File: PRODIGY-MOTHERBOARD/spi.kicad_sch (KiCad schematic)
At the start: 0 parts

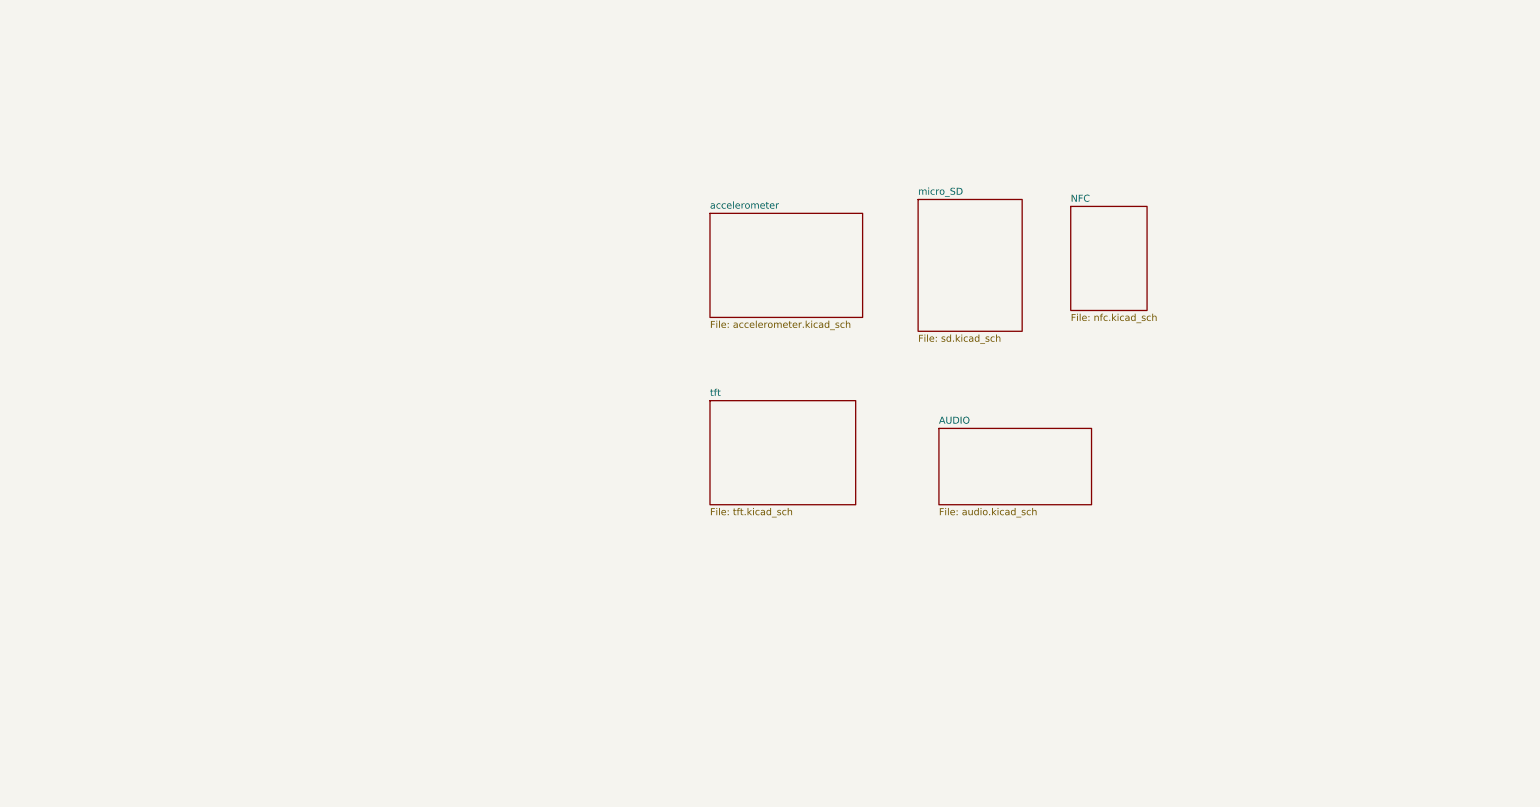
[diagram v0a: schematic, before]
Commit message: Finished I2C device and bus schematics. Added logic level translation.
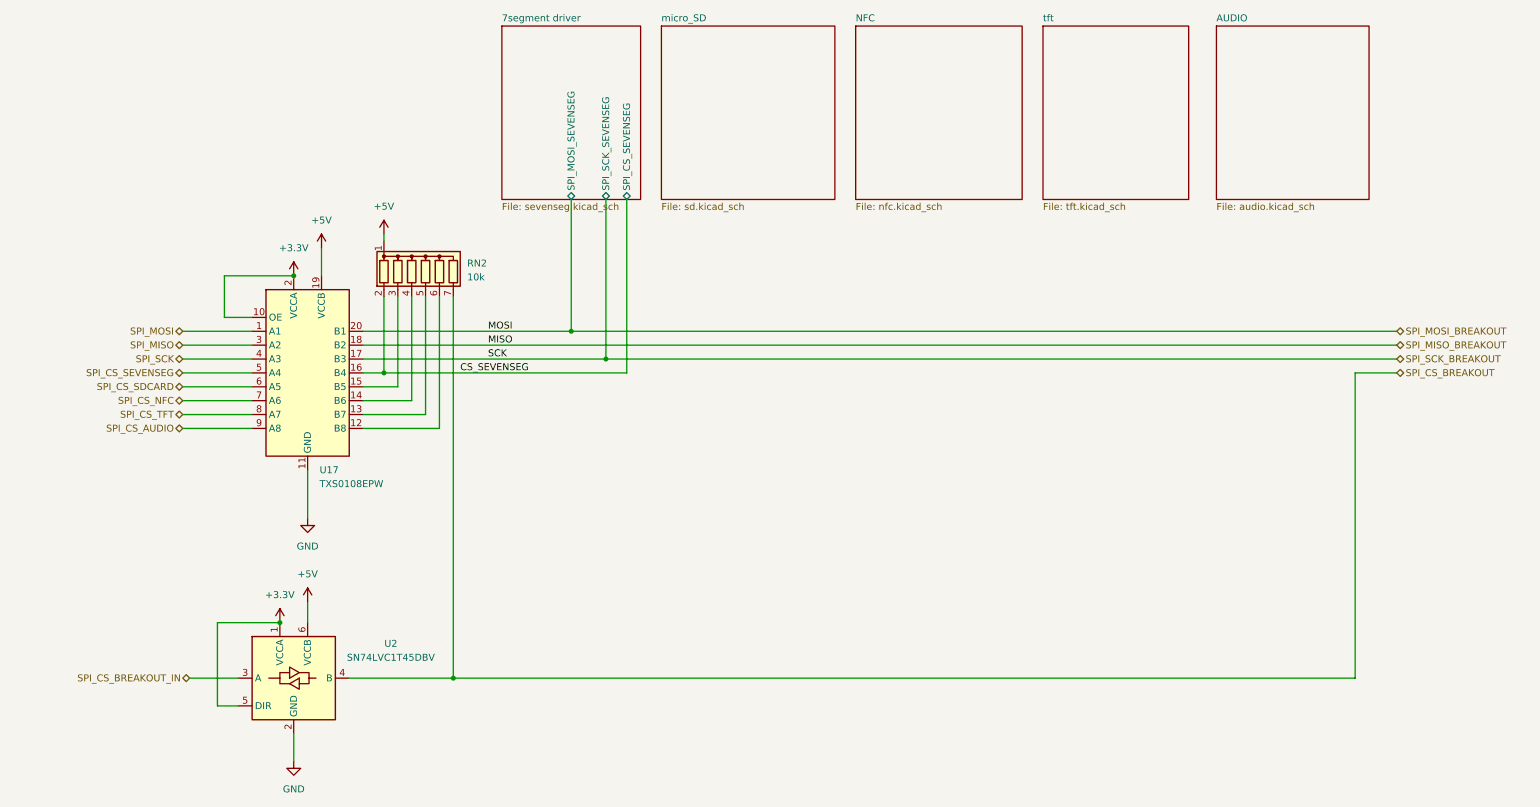
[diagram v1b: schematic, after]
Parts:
- added RN2: 10k, Resistor_SMD:R_Array_Convex_4x0603, symbol Device:R_Network06
- added U17: TXS0108EPW, Package_SO:TSSOP-20_4.4x6.5mm_P0.65mm, symbol Logic_LevelTranslator:TXS0108EPW
- added U2: SN74LVC1T45DBV, Package_TO_SOT_SMD:SOT-23-6, symbol Logic_LevelTranslator:SN74LVC1T45DBV
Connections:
- new net: RN2.6 (R5), U17.12 (B8)
- new net: RN2.5 (R4), U17.13 (B7)
- new net: RN2.4 (R3), U17.14 (B6)
- new net: RN2.3 (R2), U17.15 (B5)
- new net +3.3V: U17.10 (OE), U17.2 (VCCA), U2.1 (VCCA), U2.5 (DIR)
- new net +5V: RN2.1 (common), U17.19 (VCCB), U2.6 (VCCB)
- new net CS_SEVENSEG: RN2.2 (R1), U17.16 (B4)
- new net GND: U17.11 (GND), U2.2 (GND)
- new net SPI_CS_AUDIO: U17.9 (A8)
- new net SPI_CS_BREAKOUT: RN2.7 (R6), U2.4 (B)
- new net SPI_CS_BREAKOUT_IN: U2.3 (A)
- new net SPI_CS_NFC: U17.7 (A6)
- new net SPI_CS_SDCARD: U17.6 (A5)
- new net SPI_CS_SEVENSEG: U17.5 (A4)
- new net SPI_CS_TFT: U17.8 (A7)
- new net SPI_MISO: U17.3 (A2)
- new net SPI_MISO_BREAKOUT: U17.18 (B2)
- new net SPI_MOSI: U17.1 (A1)
- new net SPI_MOSI_BREAKOUT: U17.20 (B1)
- new net SPI_SCK: U17.4 (A3)
- new net SPI_SCK_BREAKOUT: U17.17 (B3)
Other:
- removed sheet accelerometer
- added sheet 7segment driver (sevenseg.kicad_sch)

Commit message: SPI SD CARD circuit added.
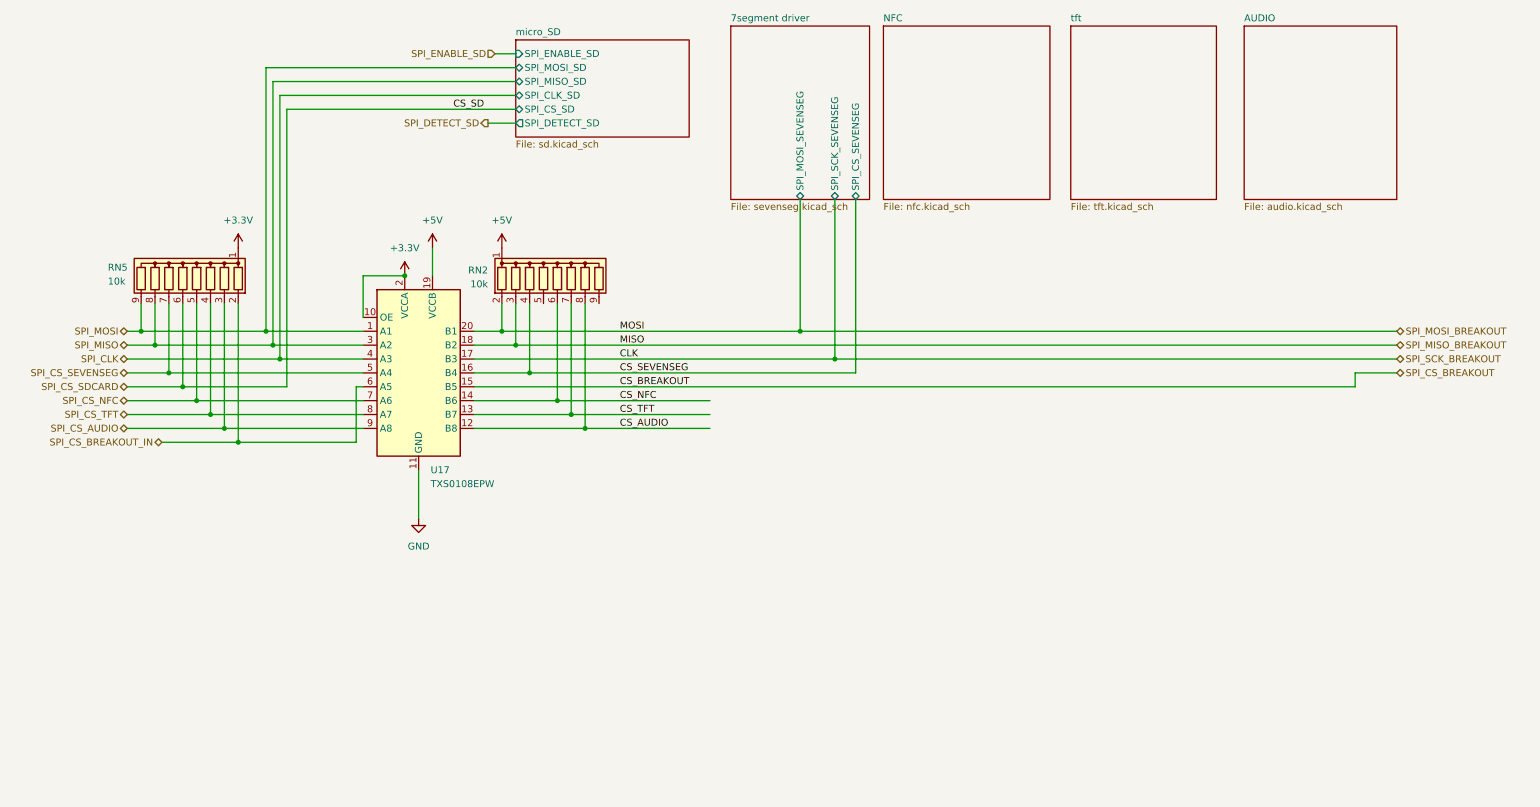
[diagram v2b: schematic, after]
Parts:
- removed RN2: 10k, Resistor_SMD:R_Array_Convex_4x0603, symbol Device:R_Network06
- removed U2: SN74LVC1T45DBV, Package_TO_SOT_SMD:SOT-23-6, symbol Logic_LevelTranslator:SN74LVC1T45DBV
- added RN2, RN5: 10k, Resistor_SMD:R_Array_Convex_5x0603, symbol Device:R_Network08
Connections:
- net +3.3V: now also RN5.1 (common)
- net +5V: now also RN2.1 (common)
- net CS_SEVENSEG: now also RN2.4 (R3)
- net SPI_CS_AUDIO: now also RN5.3 (R2)
- net SPI_CS_BREAKOUT: now also U17.15 (B5)
- net SPI_CS_BREAKOUT_IN: now also U17.6 (A5), RN5.2 (R1)
- net SPI_CS_NFC: now also RN5.5 (R4)
- net SPI_CS_SDCARD: now also RN5.6 (R5); no longer U17.6 (A5)
- net SPI_CS_SEVENSEG: now also RN5.7 (R6)
- net SPI_CS_TFT: now also RN5.4 (R3)
- net SPI_MISO: now also RN5.8 (R7)
- net SPI_MISO_BREAKOUT: now also RN2.3 (R2)
- net SPI_MOSI: now also RN5.9 (R8)
- net SPI_MOSI_BREAKOUT: now also RN2.2 (R1)
- net CS_AUDIO: now reaches U17.12 (B8)
- net CS_AUDIO: now also RN2.8 (R7)
- net CS_TFT: now reaches U17.13 (B7)
- net CS_TFT: now also RN2.7 (R6)
- net CS_NFC: now reaches U17.14 (B6)
- net CS_NFC: now also RN2.6 (R5)
- net SPI_SCK renamed SPI_CLK
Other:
- sheet micro_SD ports: added SPI_CLK_SD, SPI_CS_SD, SPI_DETECT_SD, SPI_ENABLE_SD, SPI_MISO_SD, SPI_MOSI_SD; removed none
- moved on the sheet: U17

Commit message: Finished neopixel and button's schematic.
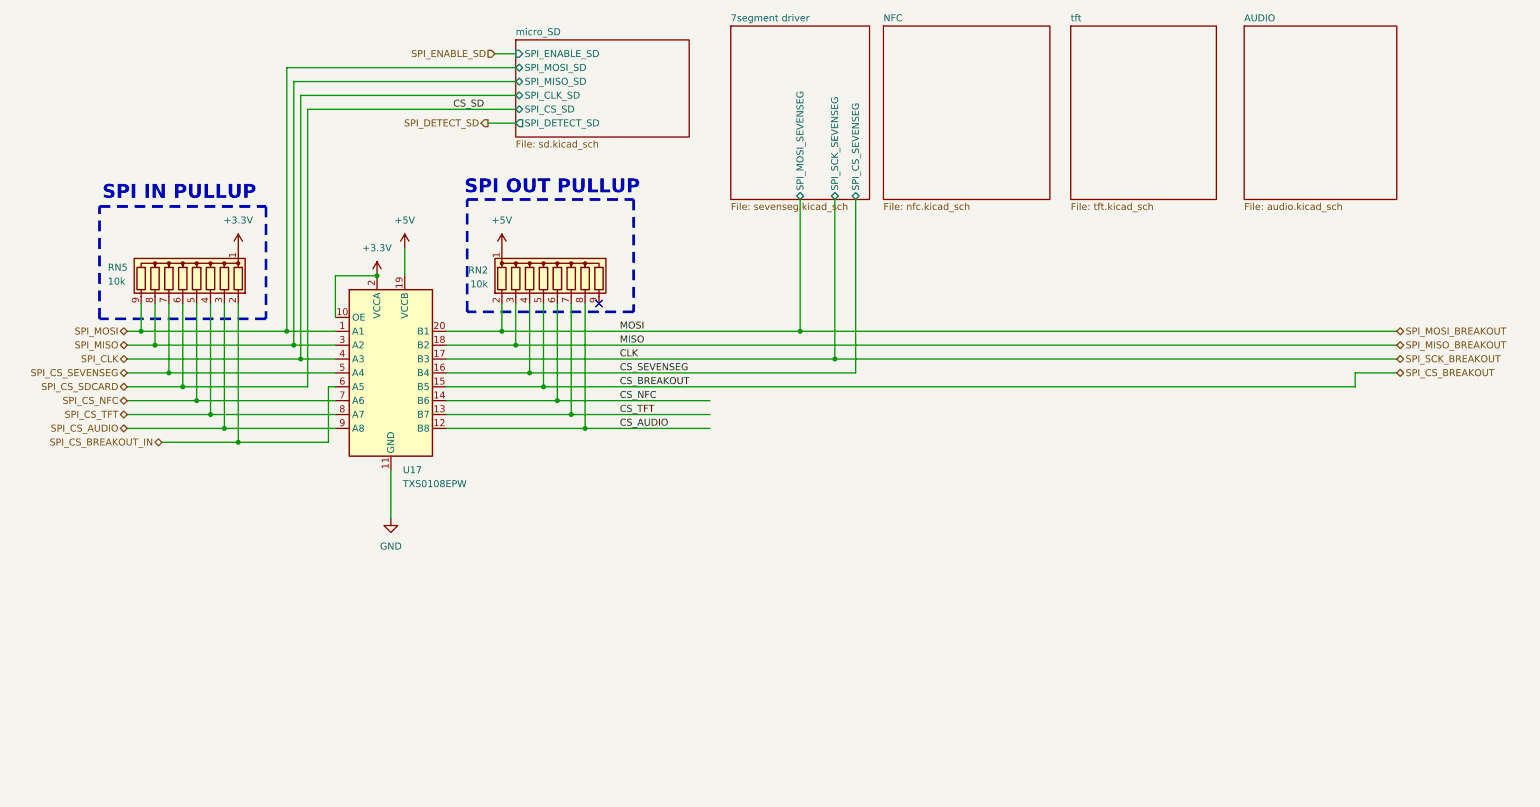
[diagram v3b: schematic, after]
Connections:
- net SPI_CS_BREAKOUT: now also RN2.5 (R4)
- no-connect marks 0 -> 1
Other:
- note added: "SPI IN PULLUP"
- note added: "SPI OUT PULLUP"
- moved on the sheet: U17

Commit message: CAN schematic done
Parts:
- renumbered RN5 to RN1, U17 to U15
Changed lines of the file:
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@@
 		(dnp no)
 		(fields_autoplaced yes)
-		(property "Reference" "#PWR031"
+		(property "Reference" "#PWR061"
 			(at 73.66 83.82 0)
 			(effects
@@
 			(project "PRODIGY-MOTHERBOARD"
 				(path "/f1c25860-8989-4190-bd24-2491d23ca7d9/e2913798-f444-47a6-8b64-53020d7d816b"
-					(reference "#PWR031")
+					(reference "#PWR061")
 					(unit 1)
 				)
@@
 		(dnp no)
 		(fields_autoplaced yes)
-		(property "Reference" "#PWR030"
+		(property "Reference" "#PWR063"
 			(at 78.74 78.74 0)
 			(effects
@@
 			(project "PRODIGY-MOTHERBOARD"
 				(path "/f1c25860-8989-4190-bd24-2491d23ca7d9/e2913798-f444-47a6-8b64-53020d7d816b"
-					(reference "#PWR030")
+					(reference "#PWR063")
 					(unit 1)
 				)
@@
 		(dnp no)
 		(fields_autoplaced yes)
-		(property "Reference" "U17"
+		(property "Reference" "U15"
 			(at 78.3941 115.57 0)
 			(effects
@@
 			(project "PRODIGY-MOTHERBOARD"
 				(path "/f1c25860-8989-4190-bd24-2491d23ca7d9/e2913798-f444-47a6-8b64-53020d7d816b"
-					(reference "U17")
+					(reference "U15")
 					(unit 1)
 				)
@@
 		(dnp no)
 		(fields_autoplaced yes)
-		(property "Reference" "#PWR078"
+		(property "Reference" "#PWR060"
 			(at 48.26 78.74 0)
 			(effects
@@
 			(project "PRODIGY-MOTHERBOARD"
 				(path "/f1c25860-8989-4190-bd24-2491d23ca7d9/e2913798-f444-47a6-8b64-53020d7d816b"
-					(reference "#PWR078")
+					(reference "#PWR060")
 					(unit 1)
 				)
@@
 		(dnp no)
 		(fields_autoplaced yes)
-		(property "Reference" "#PWR029"
+		(property "Reference" "#PWR062"
 			(at 76.2 130.81 0)
 			(effects
@@
 			(project "PRODIGY-MOTHERBOARD"
 				(path "/f1c25860-8989-4190-bd24-2491d23ca7d9/e2913798-f444-47a6-8b64-53020d7d816b"
-					(reference "#PWR029")
+					(reference "#PWR062")
 					(unit 1)
 				)
@@
 		(dnp no)
 		(fields_autoplaced yes)
-		(property "Reference" "#PWR026"
+		(property "Reference" "#PWR064"
 			(at 96.52 78.74 0)
 			(effects
@@
 			(project "PRODIGY-MOTHERBOARD"
 				(path "/f1c25860-8989-4190-bd24-2491d23ca7d9/e2913798-f444-47a6-8b64-53020d7d816b"
-					(reference "#PWR026")
+					(reference "#PWR064")
 					(unit 1)
 				)
@@
 		(on_board yes)
 		(dnp no)
-		(property "Reference" "RN5"
+		(property "Reference" "RN1"
 			(at 24.384 78.486 0)
 			(effects
@@
 			(project "PRODIGY-MOTHERBOARD"
 				(path "/f1c25860-8989-4190-bd24-2491d23ca7d9/e2913798-f444-47a6-8b64-53020d7d816b"
-					(reference "RN5")
-					(unit 1)
-				)
+					(reference "RN1")
+					(unit 1)
+				)

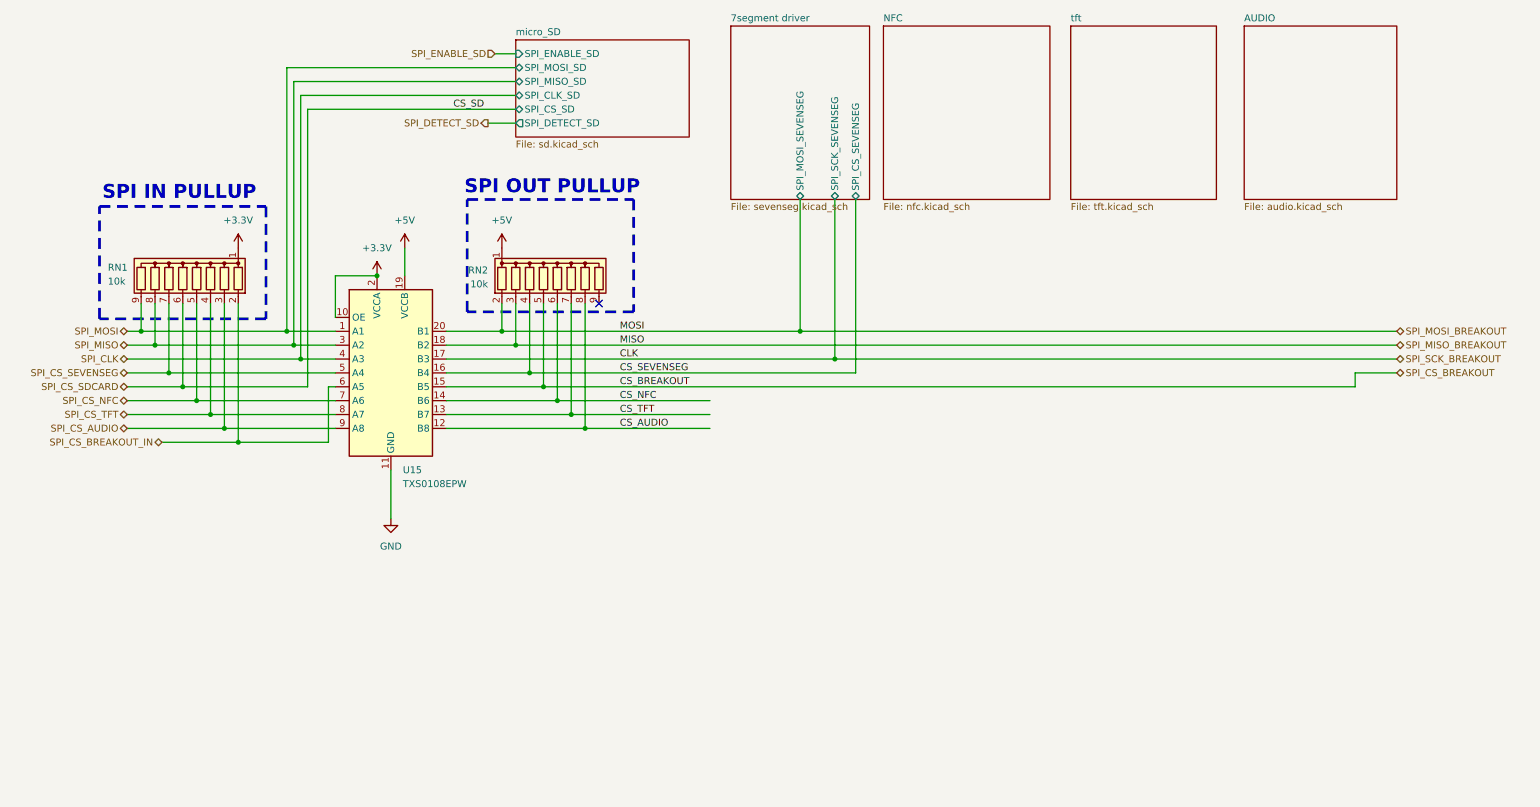
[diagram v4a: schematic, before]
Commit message: SPI NFC schematic done.
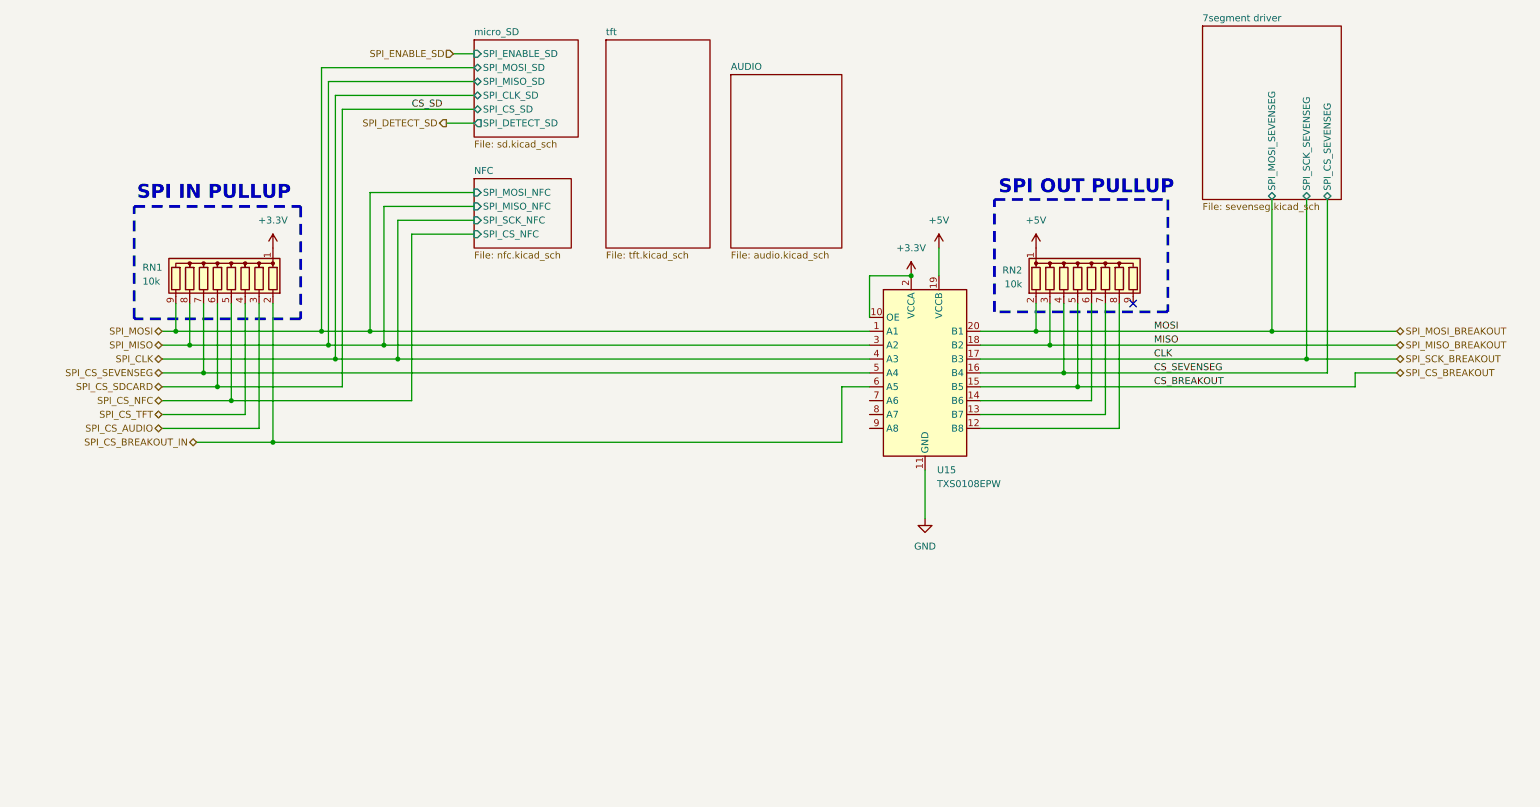
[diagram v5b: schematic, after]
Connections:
- net SPI_CS_AUDIO: no longer U15.9 (A8)
- net SPI_CS_NFC: no longer U15.7 (A6)
- net SPI_CS_TFT: no longer U15.8 (A7)
- net CS_AUDIO: no longer names the net of RN2.8 (R7), U15.12 (B8)
- net CS_NFC: no longer names the net of RN2.6 (R5), U15.14 (B6)
- net CS_TFT: no longer names the net of RN2.7 (R6), U15.13 (B7)
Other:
- sheet NFC ports: added SPI_CS_NFC, SPI_MISO_NFC, SPI_MOSI_NFC, SPI_SCK_NFC; removed none
- moved on the sheet: RN1, RN2, U15
